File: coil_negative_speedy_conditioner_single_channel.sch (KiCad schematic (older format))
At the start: 8 parts, among them J1 Conn_02x04_Counter_Clockwise, U1 4N25

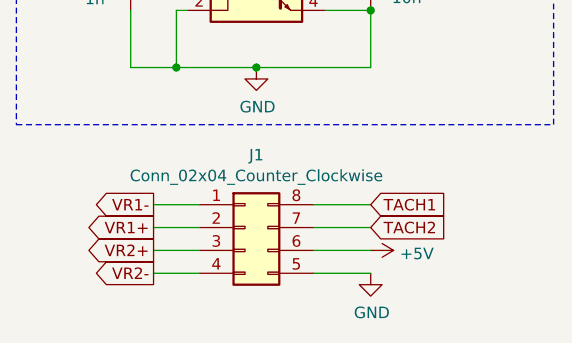
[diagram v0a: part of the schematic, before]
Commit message: VCC and GND flipped around
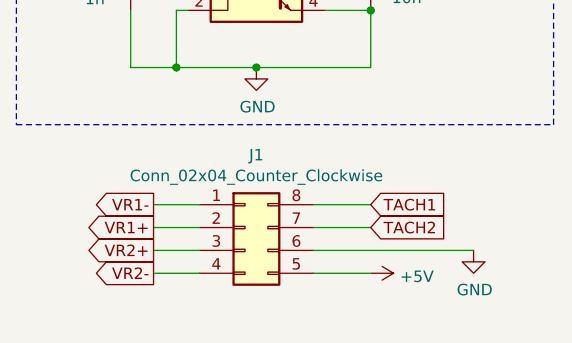
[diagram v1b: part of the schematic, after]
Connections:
- net +5V: now also J1.5 (Pin_5); no longer J1.6 (Pin_6)
- net GND: now also J1.6 (Pin_6); no longer J1.5 (Pin_5)
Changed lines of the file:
@@
 L power:+5V #PWR0103
 U 1 1 604BEB12
-P 5450 4200
-F 0 "#PWR0103" H 5450 4050 50  0001 C CNN
-F 1 "+5V" V 5465 4328 50  0000 L CNN
-F 2 "" H 5450 4200 50  0001 C CNN
-F 3 "" H 5450 4200 50  0001 C CNN
-	1    5450 4200
+P 5450 4300
+F 0 "#PWR0103" H 5450 4150 50  0001 C CNN
+F 1 "+5V" V 5465 4428 50  0000 L CNN
+F 2 "" H 5450 4300 50  0001 C CNN
+F 3 "" H 5450 4300 50  0001 C CNN
+	1    5450 4300
 	0    1    1    0
 $EndComp
@@
 L power:GND #PWR0104
 U 1 1 604BF808
-P 5450 4300
-F 0 "#PWR0104" H 5450 4050 50  0001 C CNN
-F 1 "GND" H 5455 4127 50  0000 C CNN
-F 2 "" H 5450 4300 50  0001 C CNN
-F 3 "" H 5450 4300 50  0001 C CNN
-	1    5450 4300
+P 5900 4200
+F 0 "#PWR0104" H 5900 3950 50  0001 C CNN
+F 1 "GND" H 5905 4027 50  0000 C CNN
+F 2 "" H 5900 4200 50  0001 C CNN
+F 3 "" H 5900 4200 50  0001 C CNN
+	1    5900 4200
 	1    0    0    -1
 $EndComp
-Wire Wire Line
-	5200 4200 5450 4200
 Wire Wire Line
 	5200 4300 5450 4300
@@
 Text Notes 3400 4150 0    50   ~ 0
 VRx- unused\n
+Wire Wire Line
+	5200 4200 5900 4200
 $EndSCHEMATC
